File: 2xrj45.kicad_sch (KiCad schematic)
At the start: 31 parts, among them J1 Bus_RJ45_JTH-0024NL, J2 Bus_RJ45_JTH-0024NL

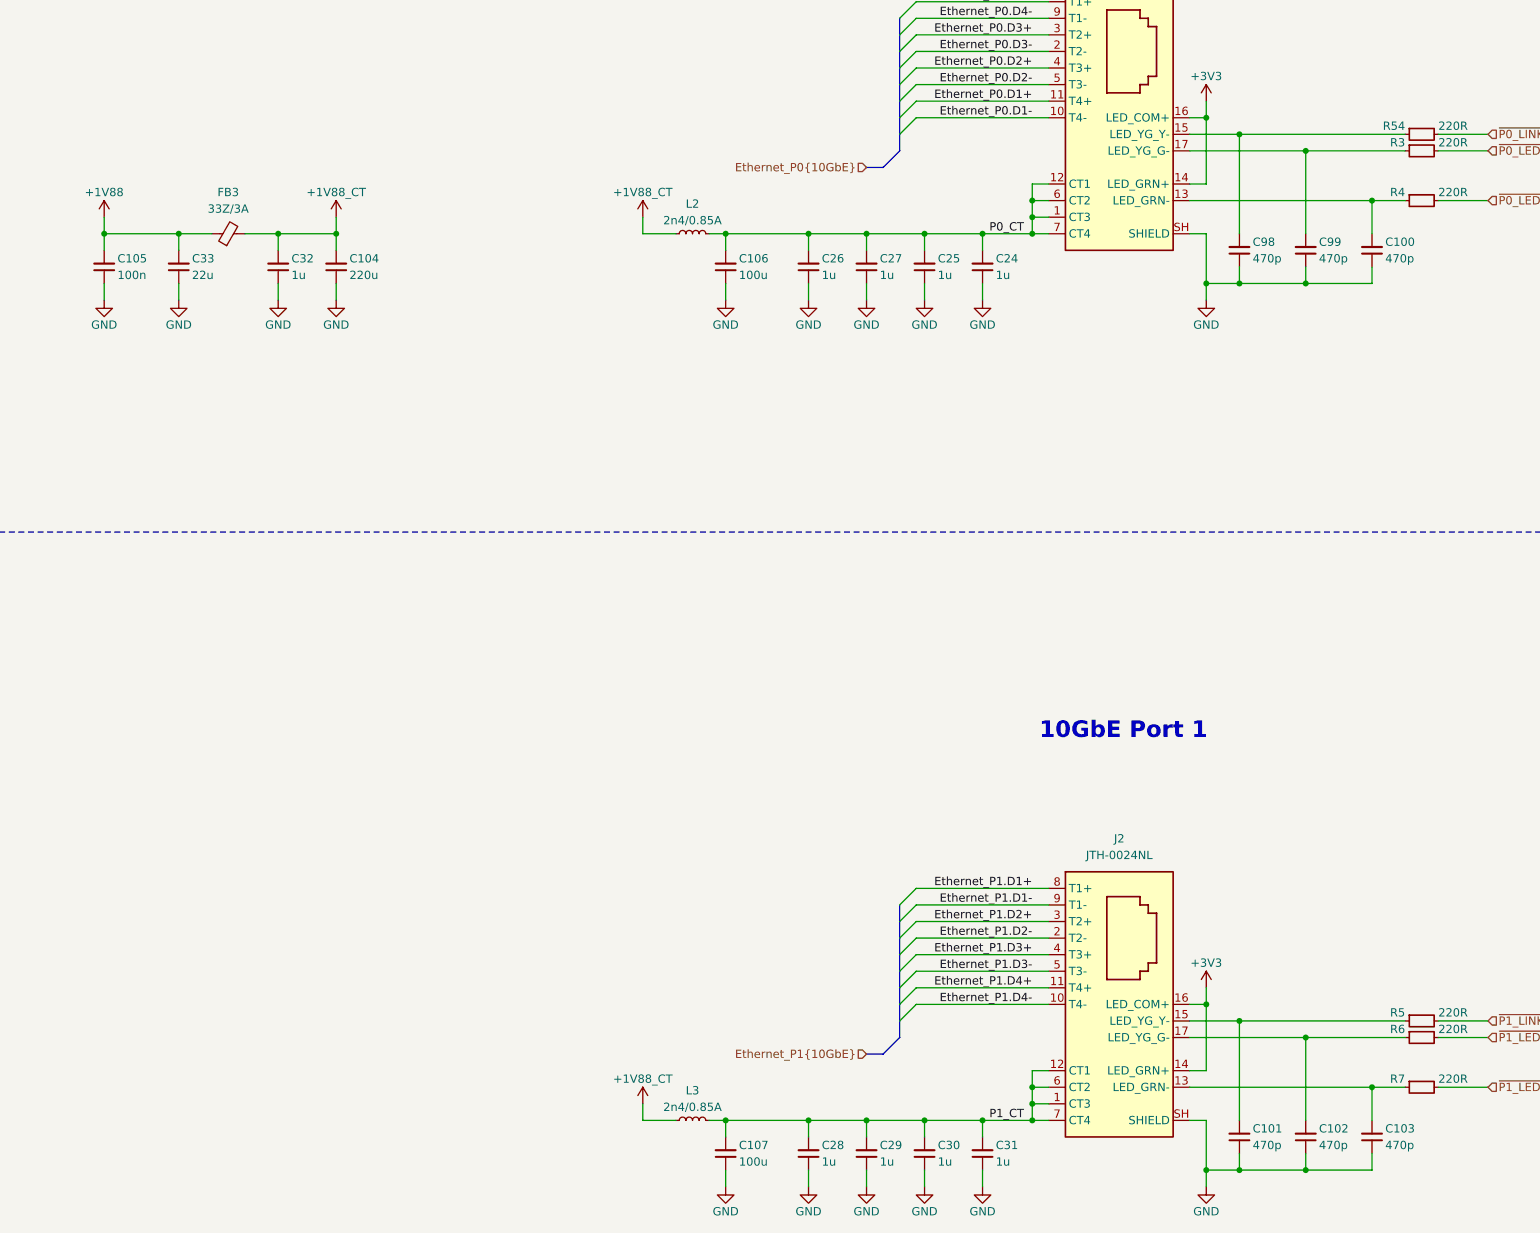
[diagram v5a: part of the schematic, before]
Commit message: [#80813] Add OCuLink connector
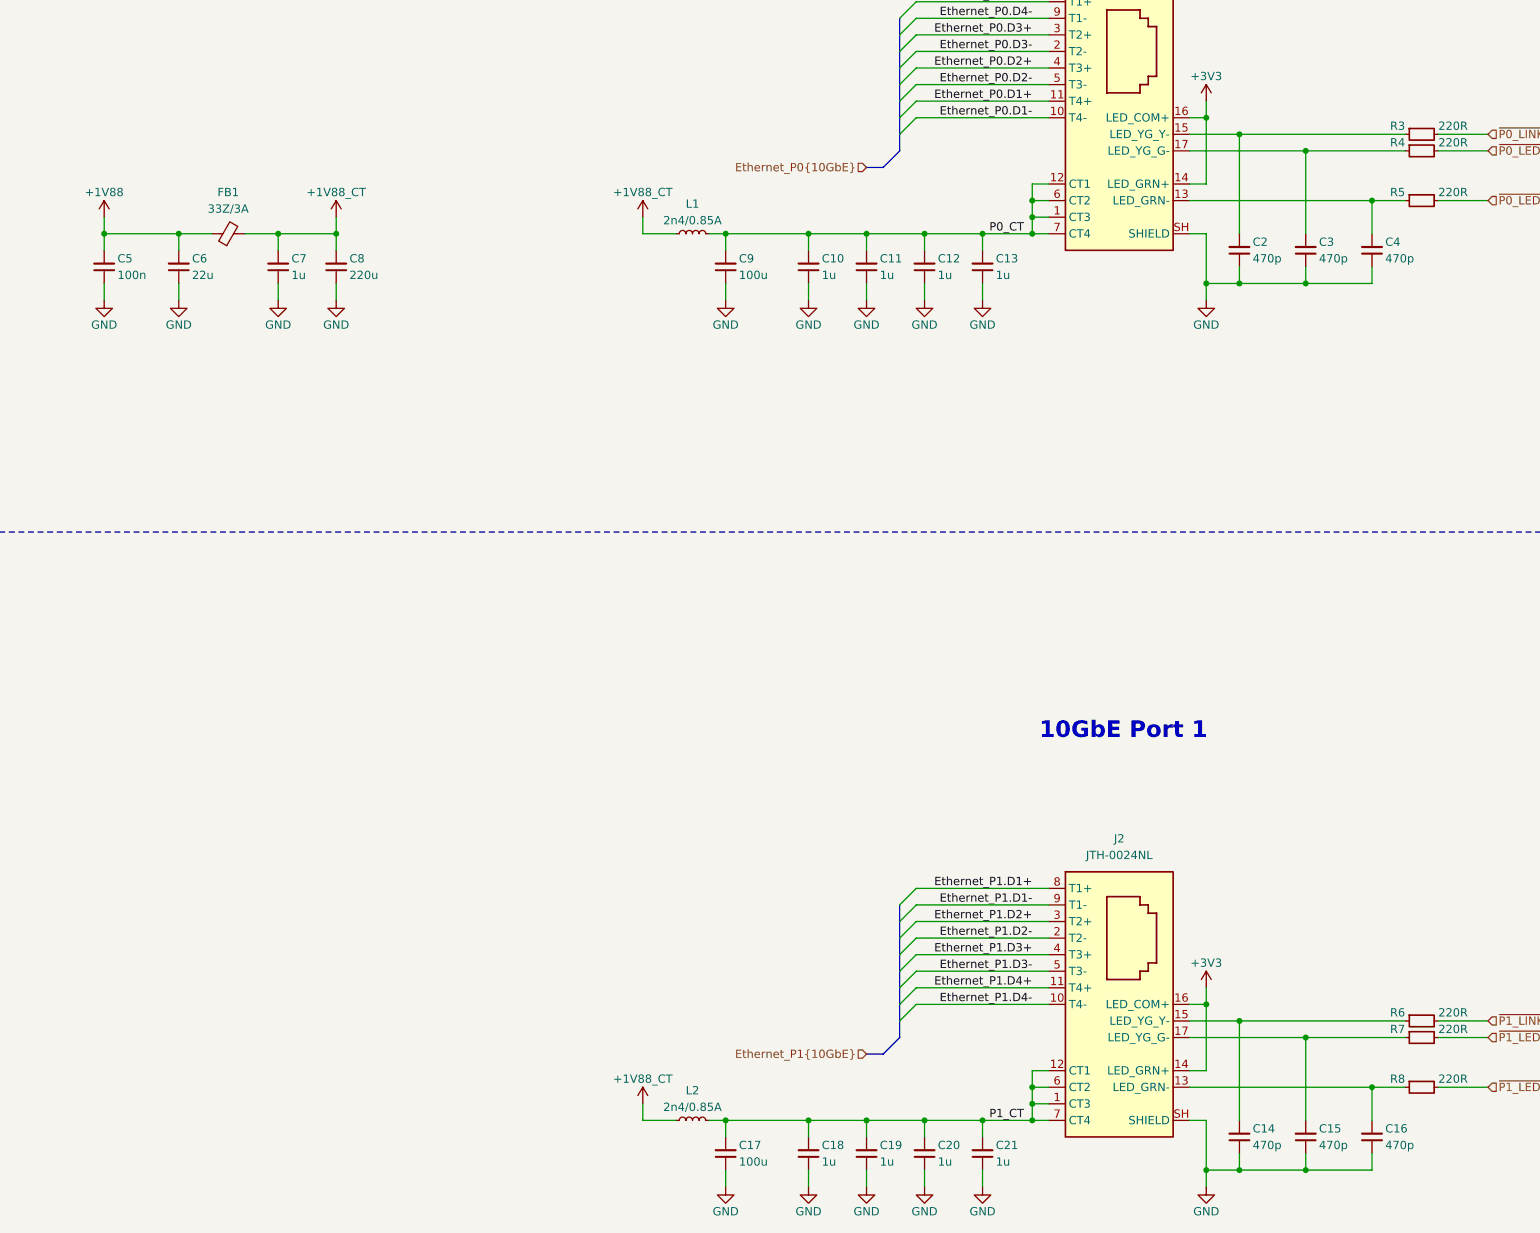
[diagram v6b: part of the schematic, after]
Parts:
- renumbered C26 to C10, C27 to C11, C25 to C12, C24 to C13, C101 to C14, C102 to C15, C103 to C16, C107 to C17, C28 to C18, C29 to C19, C98 to C2, C30 to C20, C31 to C21, C99 to C3, C100 to C4, C105 to C5, C33 to C6, C32 to C7, C104 to C8, C106 to C9, FB3 to FB1, L2 to L1, L3 to L2, R54 to R3, R3 to R4, R4 to R5, R5 to R6, R6 to R7, R7 to R8

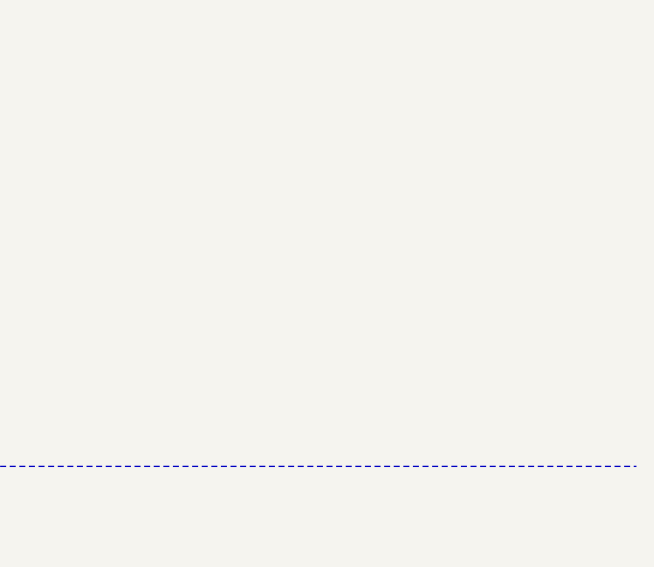
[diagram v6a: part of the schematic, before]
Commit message: [#80813] Add power input connectors, heatsink, mounting, draft component placement
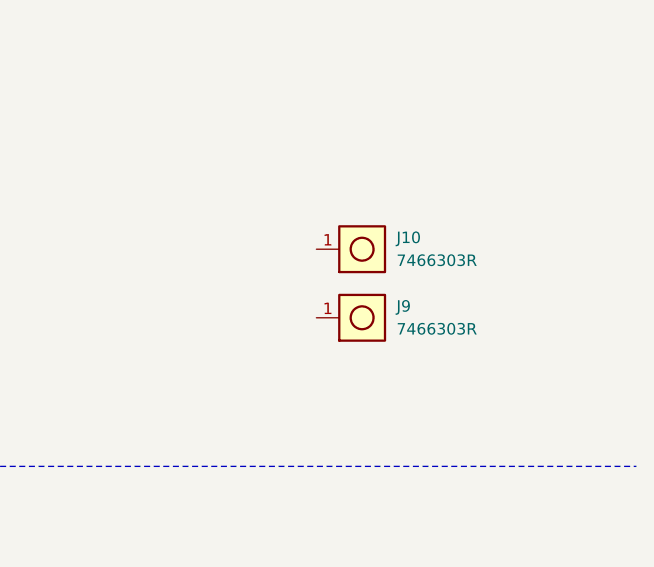
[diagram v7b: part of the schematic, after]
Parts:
- added J10, J9: MP_Terminal_M3_SMD_7466303R, antmicro-footprints:MP_Terminal_M3_SMD_7466303R, symbol antmicroMechanicalParts:MP_Terminal_M3_SMD_7466303R
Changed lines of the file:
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@@
+	)
+	(symbol
+		(lib_id "antmicroMechanicalParts:MP_Terminal_M3_SMD_7466303R")
+		(at 372.11 127 0)
+		(unit 1)
+		(exclude_from_sim no)
+		(in_bom yes)
+		(on_board yes)
+		(dnp no)
+		(fields_autoplaced yes)
+		(property "Reference" "J9"
+			(at 381 125.73 0)
+			(effects
+				(font
+					(size 1.27 1.27)
+					(thickness 0.15)
+				)
+				(justify left)
+			)
+		)
+		(property "Value" "MP_Terminal_M3_SMD_7466303R"
+			(at 394.97 134.62 0)
+			(effects
+				(font
+					(size 1.27 1.27)
+					(thickness 0.15)
+				)
+				(justify left bottom)
+				(hide yes)
+			)
+		)
+		(property "Footprint" "antmicro-footprints:MP_Terminal_M3_SMD_7466303R"
+			(at 394.97 137.16 0)
+			(effects
+				(font
+					(size 1.27 1.27)
+					(thickness 0.15)
+				)
+				(justify left bottom)
+				(hide yes)
+			)
+		)
+		(property "Datasheet" "https://www.mouser.com/datasheet/2/445/7466303-2890962.pdf"
+			(at 394.97 139.7 0)
+			(effects
+				(font
+					(size 1.27 1.27)
+					(thickness 0.15)
+				)
+				(justify left bottom)
+				(hide yes)
+			)
+		)
+		(property "Description" "PCB Terminal, 90° SMT Block, Brass, Tin, REDCUBE WP-SMRA"
+			(at 372.11 127 0)
+			(effects
+				(font
+					(size 1.27 1.27)
+				)
+				(hide yes)
+			)
+		)
+		(property "MPN" "7466303R"
+			(at 381 128.27 0)
+			(effects
+				(font
+					(size 1.27 1.27)
+					(thickness 0.15)
+				)
+				(justify left)
+			)
+		)
+		(property "Manufacturer" "Würth Elektronik"
+			(at 394.97 142.24 0)
+			(effects
+				(font
+					(size 1.27 1.27)
+					(thickness 0.15)
+				)
+				(justify left bottom)
+				(hide yes)
+			)
+		)
+		(property "Author" "Antmicro"
+			(at 394.97 144.78 0)
+			(effects
+				(font
+					(size 1.27 1.27)
+					(thickness 0.15)
+				)
+				(justify left bottom)
+				(hide yes)
+			)
+		)
+		(property "License" "Apache-2.0"
+			(at 394.97 147.32 0)
+			(effects
+				(font
+					(size 1.27 1.27)
+					(thickness 0.15)
+				)
+				(justify left bottom)
+				(hide yes)
+			)
+		)
+		(pin "1"
+		)
+		(instances
+			(project "10-gbe-expansion"
+				(path "/04bda987-e5eb-48b4-9e90-d8211dc11b39/b3dd2e9f-aefc-4b19-a6a4-069fdee319cd"
+					(reference "J9")
+					(unit 1)
+				)
+			)
+		)
 	)
 	(symbol
@@
 					(unit 1)
 				)
+			)
+		)
+	)
+	(symbol
+		(lib_id "antmicroMechanicalParts:MP_Terminal_M3_SMD_7466303R")
+		(at 372.11 119.38 0)
+		(unit 1)
+		(exclude_from_sim no)
+		(in_bom yes)
+		(on_board yes)
+		(dnp no)
+		(fields_autoplaced yes)
+		(property "Reference" "J10"
+			(at 381 118.11 0)
+			(effects
+				(font
+					(size 1.27 1.27)
+					(thickness 0.15)
+				)
+				(justify left)
+			)
+		)
+		(property "Value" "MP_Terminal_M3_SMD_7466303R"
+			(at 394.97 127 0)
+			(effects
+				(font
+					(size 1.27 1.27)
+					(thickness 0.15)
+				)
+				(justify left bottom)
+				(hide yes)
+			)
+		)
+		(property "Footprint" "antmicro-footprints:MP_Terminal_M3_SMD_7466303R"
+			(at 394.97 129.54 0)
+			(effects
+				(font
+					(size 1.27 1.27)
+					(thickness 0.15)
+				)
+				(justify left bottom)
+				(hide yes)
+			)
+		)
+		(property "Datasheet" "https://www.mouser.com/datasheet/2/445/7466303-2890962.pdf"
+			(at 394.97 132.08 0)
+			(effects
+				(font
+					(size 1.27 1.27)
+					(thickness 0.15)
+				)
+				(justify left bottom)
+				(hide yes)
+			)
+		)
+		(property "Description" "PCB Terminal, 90° SMT Block, Brass, Tin, REDCUBE WP-SMRA"
+			(at 372.11 119.38 0)
+			(effects
+				(font
+					(size 1.27 1.27)
+				)
+				(hide yes)
+			)
+		)
+		(property "MPN" "7466303R"
+			(at 381 120.65 0)
+			(effects
+				(font
+					(size 1.27 1.27)
+					(thickness 0.15)
+				)
+				(justify left)
+			)
+		)
+		(property "Manufacturer" "Würth Elektronik"
+			(at 394.97 134.62 0)
+			(effects
+				(font
+					(size 1.27 1.27)
+					(thickness 0.15)
+				)
+				(justify left bottom)
+				(hide yes)
+			)
+		)
+		(property "Author" "Antmicro"
+			(at 394.97 137.16 0)
+			(effects
+				(font
+					(size 1.27 1.27)
+					(thickness 0.15)
+				)
+				(justify left bottom)
+				(hide yes)
+			)
+		)
+		(property "License" "Apache-2.0"
+			(at 394.97 139.7 0)
+			(effects
+				(font
+					(size 1.27 1.27)
+					(thickness 0.15)
+				)
+				(justify left bottom)
+				(hide yes)
+			)
+		)
+		(pin "1"
+		)
+		(instances
+			(project "10-gbe-expansion"
+				(path "/04bda987-e5eb-48b4-9e90-d8211dc11b39/b3dd2e9f-aefc-4b19-a6a4-069fdee319cd"
+					(reference "J10")
+					(unit 1)
+				)
